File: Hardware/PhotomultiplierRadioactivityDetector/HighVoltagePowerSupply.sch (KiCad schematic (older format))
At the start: 29 parts, among them Q3 Q_NMOS_GDS, U4 LM3488

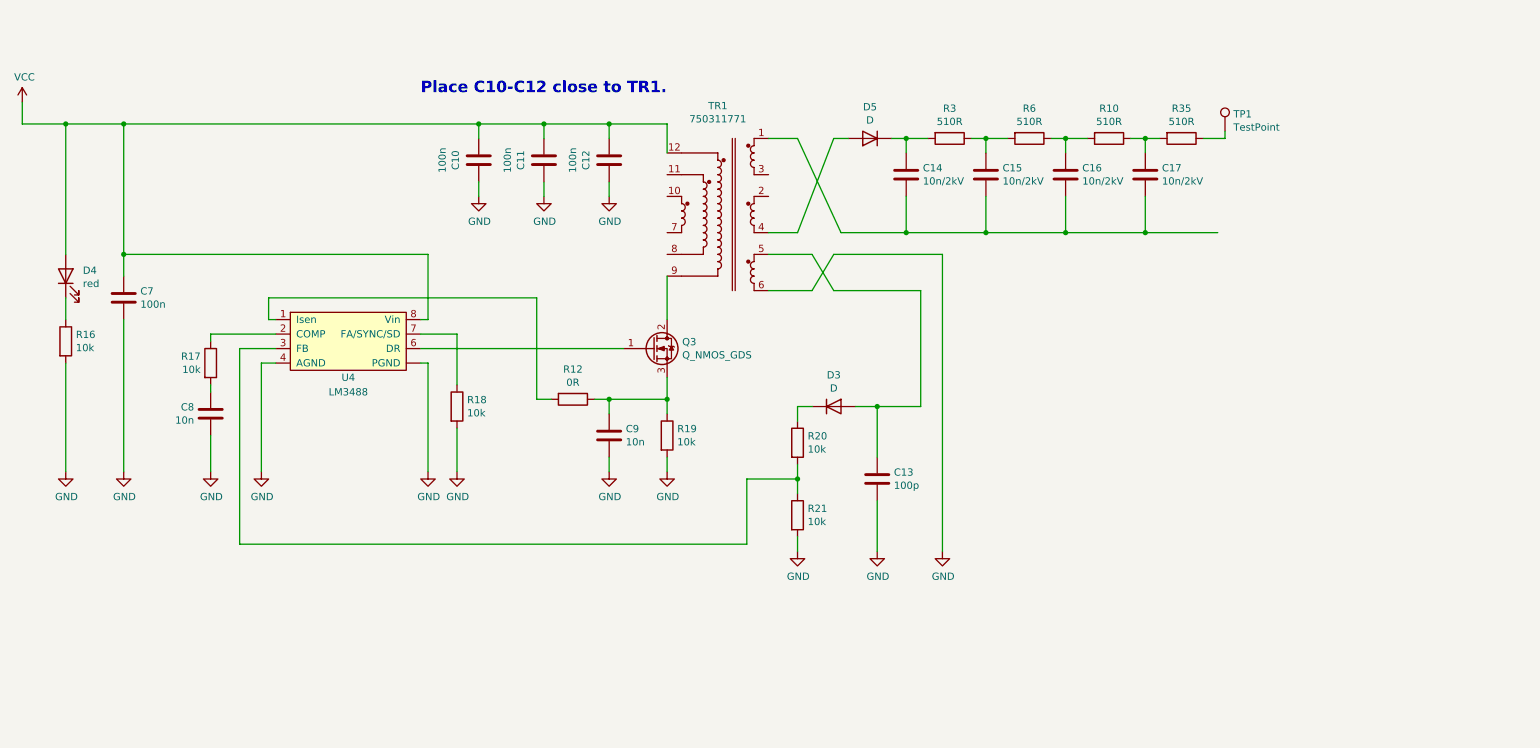
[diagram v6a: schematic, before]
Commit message: fix footprints
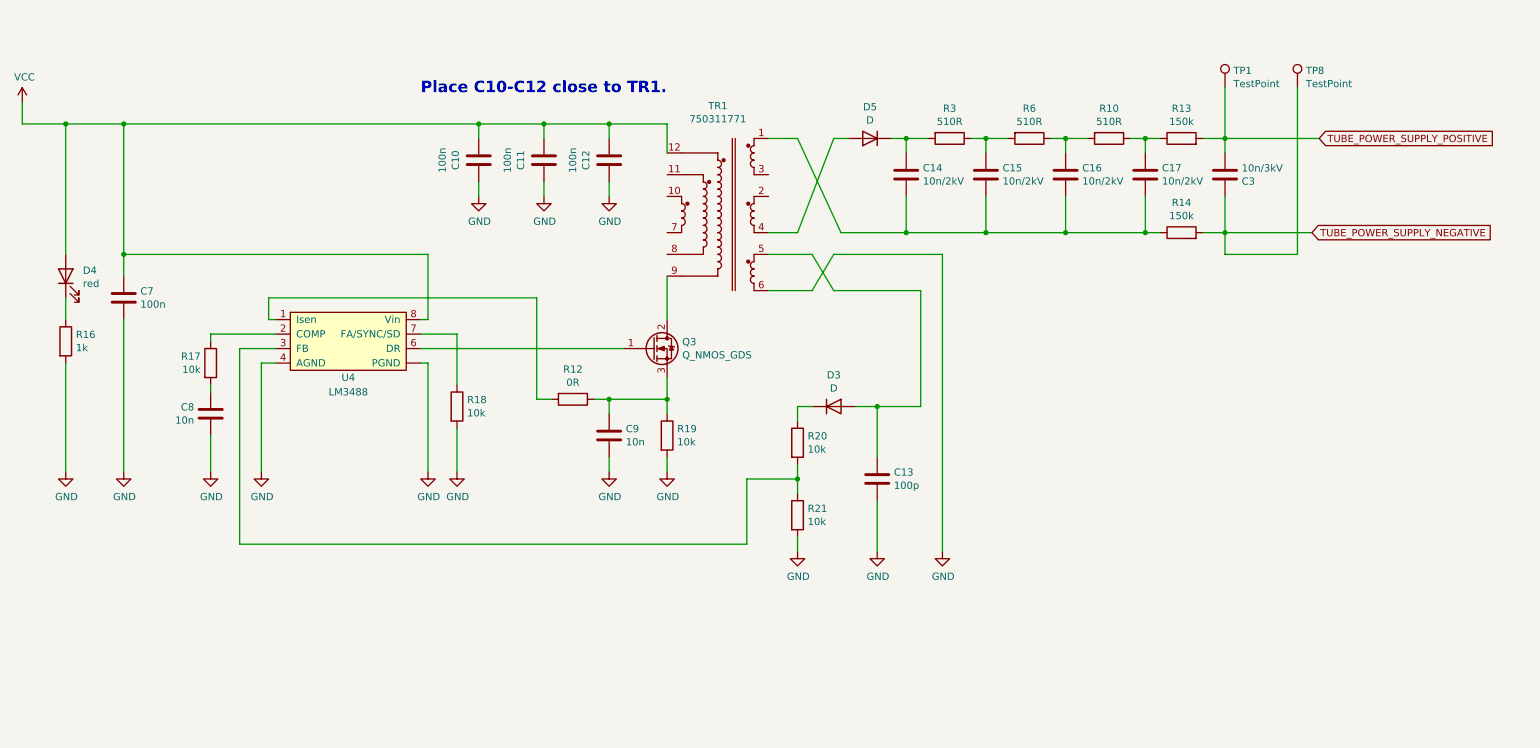
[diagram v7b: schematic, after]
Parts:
- removed R35: 510R, Resistor_SMD:R_MELF_MMB-0207, symbol Device:R
- added C3: 10n/3kV, Capacitor_THT:C_Disc_D11.0mm_W5.0mm_P7.50mm, symbol Device:C
- added R13, R14: 150k, Resistor_THT:R_Axial_DIN0411_L9.9mm_D3.6mm_P12.70mm_Horizontal, symbol Device:R
- added TP8: TestPoint, TestPoint:TestPoint_Loop_D2.60mm_Drill0.9mm_Beaded, symbol Connector:TestPoint
- D5: footprint Diode_SMD:D_MELF -> Diode_THT:D_DO-27_P15.24mm_Horizontal
- R16: value 10k -> 1k
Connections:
- net TUBE_POWER_SUPPLY_POSITIVE: now reaches TP1.1
- net TUBE_POWER_SUPPLY_POSITIVE: now also C3.2, R13.2
- net at C14.1, C15.1, C16.1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: now also R14.1
- net at C17.2, R10.1: now also R13.1
- new net TUBE_POWER_SUPPLY_NEGATIVE: C3.1, R14.2, TP8.1
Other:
- moved on the sheet: TP1
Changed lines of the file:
@@
 L Connector:TestPoint TP1
 U 1 1 5EDBC7E8
-P 9300 1950
-F 0 "TP1" H 9358 2068 50  0000 L CNN
-F 1 "TestPoint" H 9358 1977 50  0000 L CNN
-F 2 "TestPoint:TestPoint_Loop_D2.60mm_Drill0.9mm_Beaded" H 9500 1950 50  0001 C CNN
-F 3 "~" H 9500 1950 50  0001 C CNN
-	1    9300 1950
+P 9300 1650
+F 0 "TP1" H 9358 1768 50  0000 L CNN
+F 1 "TestPoint" H 9358 1677 50  0000 L CNN
+F 2 "TestPoint:TestPoint_Loop_D2.60mm_Drill0.9mm_Beaded" H 9500 1650 50  0001 C CNN
+F 3 "~" H 9500 1650 50  0001 C CNN
+	1    9300 1650
 	1    0    0    -1
 $EndComp
@@
 AR Path="/5EDA5628/5EDD7666" Ref="R16"  Part="1"
 F 0 "R16" H 1370 3446 50  0000 L CNN
-F 1 "10k" H 1370 3355 50  0000 L CNN
+F 1 "1k" H 1370 3355 50  0000 L CNN
 F 2 "Resistor_SMD:R_0805_2012Metric_Pad1.15x1.40mm_HandSolder" V 1230 3400 50  0001 C CNN
 F 3 "~" H 1300 3400 50  0001 C CNN
@@
 F 0 "D5" H 6850 1783 50  0000 C CNN
 F 1 "D" H 6850 1874 50  0000 C CNN
-F 2 "Diode_SMD:D_MELF" H 6850 2000 50  0001 C CNN
+F 2 "Diode_THT:D_DO-27_P15.24mm_Horizontal" H 6850 2000 50  0001 C CNN
 F 3 "~" H 6850 2000 50  0001 C CNN
 	1    6850 2000
@@
 Wire Wire Line
 	8200 2100 8200 2000
-Wire Wire Line
-	9300 2000 9300 1950
 Wire Wire Line
 	7100 2000 7100 2100
@@
 Wire Wire Line
 	8650 2000 8750 2000
-$Comp
-L Device:R R?
-U 1 1 5EEA3B44
-P 9000 2000
-AR Path="/5EDA53F3/5EEA3B44" Ref="R?"  Part="1"
-AR Path="/5EDA5628/5EEA3B44" Ref="R35"  Part="1"
-F 0 "R35" V 8793 2000 50  0000 C CNN
-F 1 "510R" V 8884 2000 50  0000 C CNN
-F 2 "Resistor_SMD:R_MELF_MMB-0207" V 8930 2000 50  0001 C CNN
-F 3 "~" H 9000 2000 50  0001 C CNN
-	1    9000 2000
-	0    1    1    0
-$EndComp
-Wire Wire Line
-	8750 2000 8850 2000
 Connection ~ 8750 2000
-Wire Wire Line
-	9150 2000 9300 2000
 $Comp
 L PhotomultiplierRadioactivityDetector:750311771 TR1
@@
 	-1   0    0    -1
 $EndComp
-Wire Wire Line
-	9250 2650 8750 2650
 Connection ~ 7100 2650
 Connection ~ 7650 2650
@@
 Wire Wire Line
 	8200 2650 7650 2650
-Connection ~ 8750 2650
 Wire Wire Line
 	8750 2650 8200 2650
@@
 P 4150 2400
 AR Path="/5EDA53F3/5F0C936E" Ref="#PWR?"  Part="1"
-AR Path="/5EDA5628/5F0C936E" Ref="#PWR?"  Part="1"
-F 0 "#PWR?" H 4150 2150 50  0001 C CNN
+AR Path="/5EDA5628/5F0C936E" Ref="#PWR07"  Part="1"
+F 0 "#PWR07" H 4150 2150 50  0001 C CNN
 F 1 "GND" H 4155 2227 50  0000 C CNN
 F 2 "" H 4150 2400 50  0001 C CNN
@@
 P 4600 2400
 AR Path="/5EDA53F3/5F0C9858" Ref="#PWR?"  Part="1"
-AR Path="/5EDA5628/5F0C9858" Ref="#PWR?"  Part="1"
-F 0 "#PWR?" H 4600 2150 50  0001 C CNN
+AR Path="/5EDA5628/5F0C9858" Ref="#PWR08"  Part="1"
+F 0 "#PWR08" H 4600 2150 50  0001 C CNN
 F 1 "GND" H 4605 2227 50  0000 C CNN
 F 2 "" H 4600 2400 50  0001 C CNN
@@
 P 5050 2400
 AR Path="/5EDA53F3/5F0C9B1D" Ref="#PWR?"  Part="1"
-AR Path="/5EDA5628/5F0C9B1D" Ref="#PWR?"  Part="1"
-F 0 "#PWR?" H 5050 2150 50  0001 C CNN
+AR Path="/5EDA5628/5F0C9B1D" Ref="#PWR09"  Part="1"
+F 0 "#PWR09" H 5050 2150 50  0001 C CNN
 F 1 "GND" H 5055 2227 50  0000 C CNN
 F 2 "" H 5050 2400 50  0001 C CNN
@@
 Wire Wire Line
 	5050 2400 5050 2300
+$Comp
+L Device:R R?
+U 1 1 5F0A8402
+P 9000 2000
+AR Path="/5EDA585D/5F0A8402" Ref="R?"  Part="1"
+AR Path="/5EDA5628/5F0A8402" Ref="R13"  Part="1"
+F 0 "R13" V 9207 2000 50  0000 C CNN
+F 1 "150k" V 9116 2000 50  0000 C CNN
+F 2 "Resistor_THT:R_Axial_DIN0411_L9.9mm_D3.6mm_P12.70mm_Horizontal" V 8930 2000 50  0001 C CNN
+F 3 "~" H 9000 2000 50  0001 C CNN
+	1    9000 2000
+	0    -1   -1   0
+$EndComp
+$Comp
+L Device:C C?
+U 1 1 5F0A8408
+P 9300 2250
+AR Path="/5EDA585D/5F0A8408" Ref="C?"  Part="1"
+AR Path="/5EDA5628/5F0A8408" Ref="C3"  Part="1"
+F 0 "C3" H 9185 2296 50  0000 R CNN
+F 1 "10n/3kV" H 9185 2205 50  0000 R CNN
+F 2 "Capacitor_THT:C_Disc_D11.0mm_W5.0mm_P7.50mm" H 9338 2100 50  0001 C CNN
+F 3 "~" H 9300 2250 50  0001 C CNN
+	1    9300 2250
+	-1   0    0    1
+$EndComp
+Wire Wire Line
+	9150 2000 9300 2000
+Wire Wire Line
+	9300 2100 9300 2000
+Connection ~ 9300 2000
+Wire Wire Line
+	9300 2000 9950 2000
+Text GLabel 9900 2650 2    50   Input ~ 0
+TUBE_POWER_SUPPLY_NEGATIVE
+Text GLabel 9950 2000 2    50   Input ~ 0
+TUBE_POWER_SUPPLY_POSITIVE
+Wire Wire Line
+	8750 2000 8850 2000
+$Comp
+L Device:R R?
+U 1 1 5F0CDD8A
+P 9000 2650
+AR Path="/5EDA585D/5F0CDD8A" Ref="R?"  Part="1"
+AR Path="/5EDA5628/5F0CDD8A" Ref="R14"  Part="1"
+F 0 "R14" V 9207 2650 50  0000 C CNN
+F 1 "150k" V 9116 2650 50  0000 C CNN
+F 2 "Resistor_THT:R_Axial_DIN0411_L9.9mm_D3.6mm_P12.70mm_Horizontal" V 8930 2650 50  0001 C CNN
+F 3 "~" H 9000 2650 50  0001 C CNN
+	1    9000 2650
+	0    -1   -1   0
+$EndComp
+Wire Wire Line
+	9300 2400 9300 2650
+Wire Wire Line
+	8750 2650 8850 2650
+Connection ~ 8750 2650
+Wire Wire Line
+	9150 2650 9300 2650
+Connection ~ 9300 2650
+Wire Wire Line
+	9300 2000 9300 1650
+$Comp
+L Connector:TestPoint TP8
+U 1 1 5F0E6C9A
+P 9800 1650
+F 0 "TP8" H 9858 1768 50  0000 L CNN
+F 1 "TestPoint" H 9858 1677 50  0000 L CNN
+F 2 "TestPoint:TestPoint_Loop_D2.60mm_Drill0.9mm_Beaded" H 10000 1650 50  0001 C CNN
+F 3 "~" H 10000 1650 50  0001 C CNN
+	1    9800 1650
+	1    0    0    -1
+$EndComp
+Wire Wire Line
+	9800 1650 9800 2800
+Wire Wire Line
+	9800 2800 9300 2800
+Wire Wire Line
+	9300 2800 9300 2650
+Wire Wire Line
+	9300 2650 9900 2650
 $EndSCHEMATC

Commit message: improve component placement
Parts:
- removed TP1, TP8: TestPoint, TestPoint:TestPoint_Loop_D2.60mm_Drill0.9mm_Beaded, symbol Connector:TestPoint
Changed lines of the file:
@@
-$EndComp
-$Comp
-L Connector:TestPoint TP1
-U 1 1 5EDBC7E8
-P 9300 1650
-F 0 "TP1" H 9358 1768 50  0000 L CNN
-F 1 "TestPoint" H 9358 1677 50  0000 L CNN
-F 2 "TestPoint:TestPoint_Loop_D2.60mm_Drill0.9mm_Beaded" H 9500 1650 50  0001 C CNN
-F 3 "~" H 9500 1650 50  0001 C CNN
-	1    9300 1650
-	1    0    0    -1
 $EndComp
 $Comp
@@
 Connection ~ 9300 2650
 Wire Wire Line
-	9300 2000 9300 1650
-$Comp
-L Connector:TestPoint TP8
-U 1 1 5F0E6C9A
-P 9800 1650
-F 0 "TP8" H 9858 1768 50  0000 L CNN
-F 1 "TestPoint" H 9858 1677 50  0000 L CNN
-F 2 "TestPoint:TestPoint_Loop_D2.60mm_Drill0.9mm_Beaded" H 10000 1650 50  0001 C CNN
-F 3 "~" H 10000 1650 50  0001 C CNN
-	1    9800 1650
-	1    0    0    -1
-$EndComp
-Wire Wire Line
-	9800 1650 9800 2800
-Wire Wire Line
-	9800 2800 9300 2800
-Wire Wire Line
-	9300 2800 9300 2650
-Wire Wire Line
 	9300 2650 9900 2650
